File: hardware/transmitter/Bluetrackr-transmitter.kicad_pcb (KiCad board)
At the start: 2 copper layers, 50.8 x 30.5 mm, 43 parts, among them J1 USB_C_Receptacle_USB2.0, J2 Programming_Connector, J3 Battery_Connector, Q1 CJ2333, SW1 SW_Pair, U1 MIC5205-2.5YM5, U2 MCP73831-2-OT, U3 STM32F072C8Tx, U4 DL-24N-2.4G, U5 LSM9DS1

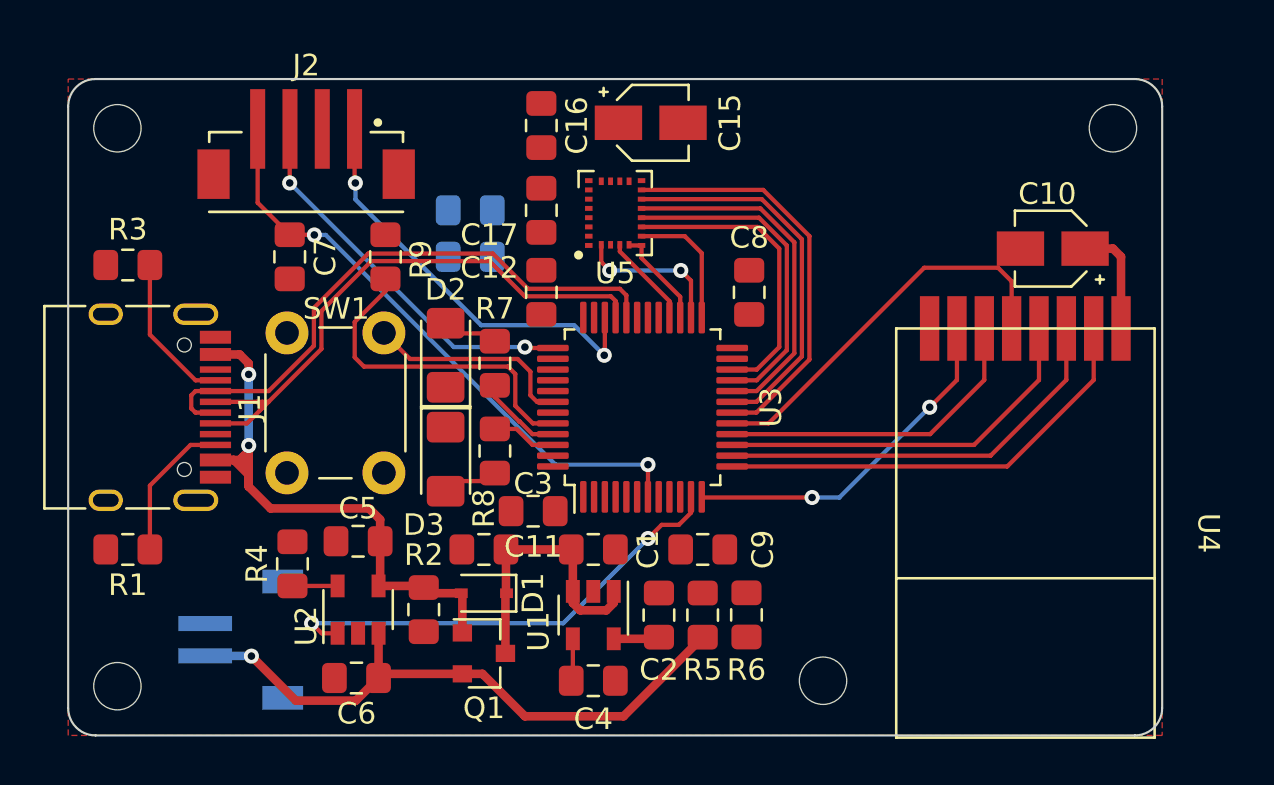
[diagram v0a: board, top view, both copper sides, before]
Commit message: Finish routing the transmitter, add DL-24N module step file
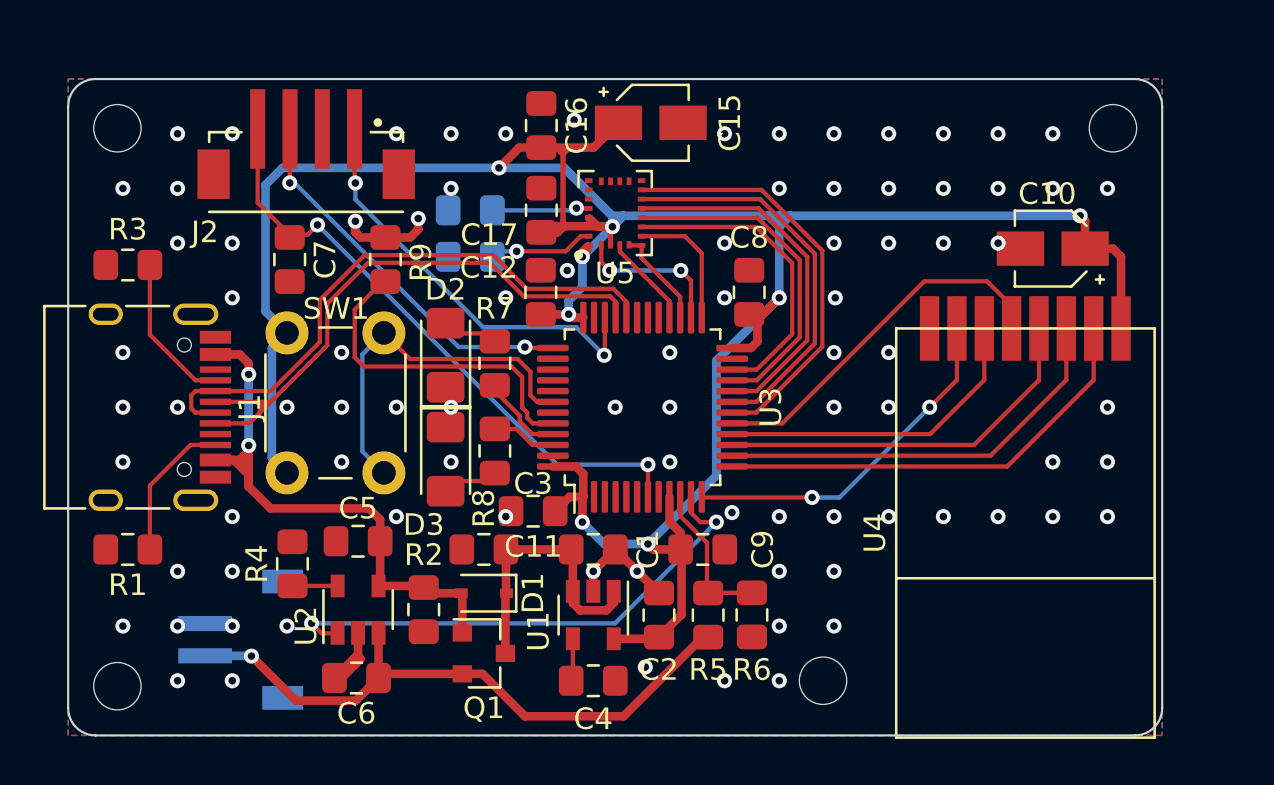
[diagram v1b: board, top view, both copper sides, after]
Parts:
- moved R5 0.25 mm to (156.7, 101.1)
- moved R6 0.25 mm to (158.8, 101.1)
- moved C7 0.13 mm to (137.3, 84.6)
- moved R9 0.13 mm to (141.7, 84.6)
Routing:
- net +2V5: track 7.29 -> 139.5 mm, vias 0 -> 8
- net GND: track 0.00 -> 13.6 mm, vias 0 -> 87
- net /BTN_PAIR: track 9.82 -> 17.1 mm
- net /BATT_SENSE: track 0.00 -> 7.04 mm
- net Net-(C14-Pad1): track 0.00 -> 4.88 mm, vias 0 -> 1
- net Net-(C13-Pad1): track 0.00 -> 4.53 mm, vias 0 -> 1
- net /CHARGE_STATUS: track 21.9 -> 24.2 mm
- net /NRF_MOSI: track 18.4 -> 17.2 mm
- net /USB_D+: track 27.5 -> 28.5 mm
- added copper zone on B.Cu, net GND

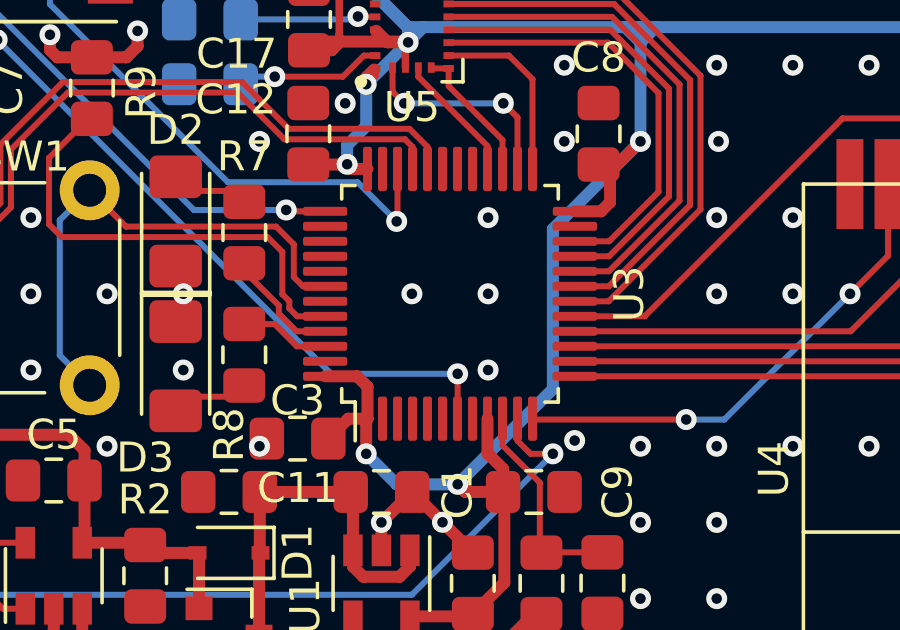
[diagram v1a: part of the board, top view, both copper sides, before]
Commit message: Correct some power traces
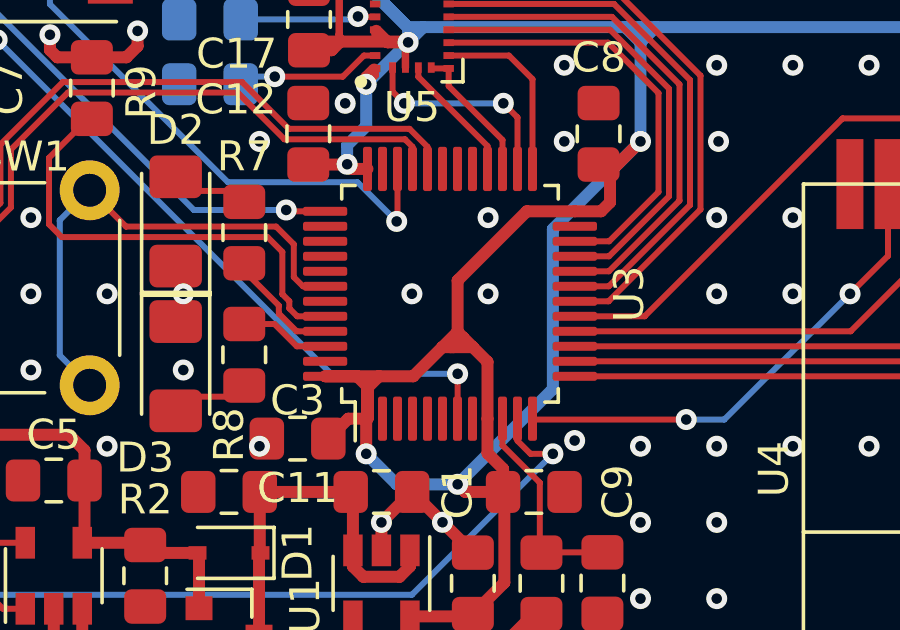
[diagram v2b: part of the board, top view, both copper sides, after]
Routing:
- net +2V5: track 139.5 -> 157.6 mm
- net GND: vias 87 -> 86
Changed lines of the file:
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@@
     (thickness 1.6)
     (drawings 13)
-    (tracks 463)
+    (tracks 479)
     (modules 43)
     (nets 56)
@@
     (arrow2b (pts (xy 127 76.2) (xy 128.126504 75.613579)))
   )
+  (segment (start 151.301 94.19) (end 152.444 94.19) (width 0.4) (layer "F.Cu") (net 3))
+  (segment (start 149.5075 94.19) (end 151.301 94.19) (width 0.4) (layer "F.Cu") (net 3))
+  (segment (start 150.92 94.571) (end 151.301 94.19) (width 0.4) (layer "F.Cu") (net 3))
+  (segment (start 150.92 95.6025) (end 150.92 94.571) (width 0.4) (layer "F.Cu") (net 3))
+  (segment (start 154.1145 92.9005) (end 154.432 93.218) (width 0.4) (layer "F.Cu") (net 3))
+  (segment (start 153.924 92.71) (end 154.1145 92.9005) (width 0.4) (layer "F.Cu") (net 3))
+  (segment (start 153.797 93.218) (end 154.1145 92.9005) (width 0.4) (layer "F.Cu") (net 3))
+  (segment (start 153.67 93.218) (end 154.432 93.218) (width 0.4) (layer "F.Cu") (net 3))
+  (segment (start 153.416 93.218) (end 153.67 93.218) (width 0.4) (layer "F.Cu") (net 3))
+  (segment (start 153.67 93.218) (end 153.797 93.218) (width 0.4) (layer "F.Cu") (net 3))
+  (segment (start 152.444 94.19) (end 153.416 93.218) (width 0.4) (layer "F.Cu") (net 3))
+  (segment (start 154.432 93.218) (end 154.92 93.706) (width 0.4) (layer "F.Cu") (net 3))
+  (segment (start 153.416 93.218) (end 153.924 92.71) (width 0.4) (layer "F.Cu") (net 3))
+  (segment (start 156.2295 88.69) (end 153.924 90.9955) (width 0.4) (layer "F.Cu") (net 3))
+  (segment (start 157.8325 88.69) (end 156.2295 88.69) (width 0.4) (layer "F.Cu") (net 3))
+  (segment (start 154.92 93.706) (end 154.92 95.6025) (width 0.4) (layer "F.Cu") (net 3))
+  (segment (start 153.924 90.9955) (end 153.924 92.71) (width 0.4) (layer "F.Cu") (net 3))
   (segment (start 158.75 100.058) (end 156.727 100.058) (width 0.2) (layer "F.Cu") (net 19))
   (segment (start 156.727 100.058) (end 156.718 100.067) (width 0.2) (layer "F.Cu") (net 19))
@@
   (via (at 175.26 93.98) (size 0.7) (drill 0.35) (layers "F.Cu" "B.Cu") (net 1))
   (via (at 172.72 93.98) (size 0.7) (drill 0.35) (layers "F.Cu" "B.Cu") (net 1))
-  (via (at 154.94 93.98) (size 0.7) (drill 0.35) (layers "F.Cu" "B.Cu") (net 1))
   (via (at 144.78 93.98) (size 0.7) (drill 0.35) (layers "F.Cu" "B.Cu") (net 1))
   (via (at 139.7 93.98) (size 0.7) (drill 0.35) (layers "F.Cu" "B.Cu") (net 1))
